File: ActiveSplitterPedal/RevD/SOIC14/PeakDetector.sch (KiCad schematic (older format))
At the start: 11 parts, among them U3 TL074

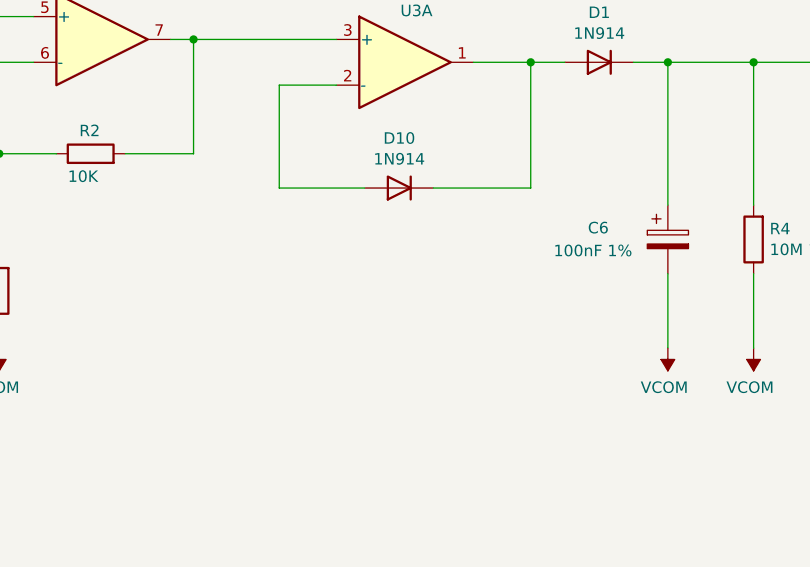
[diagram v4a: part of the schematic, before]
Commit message: updated hw
added feedback cap to peak detector (help prevent oscillation)
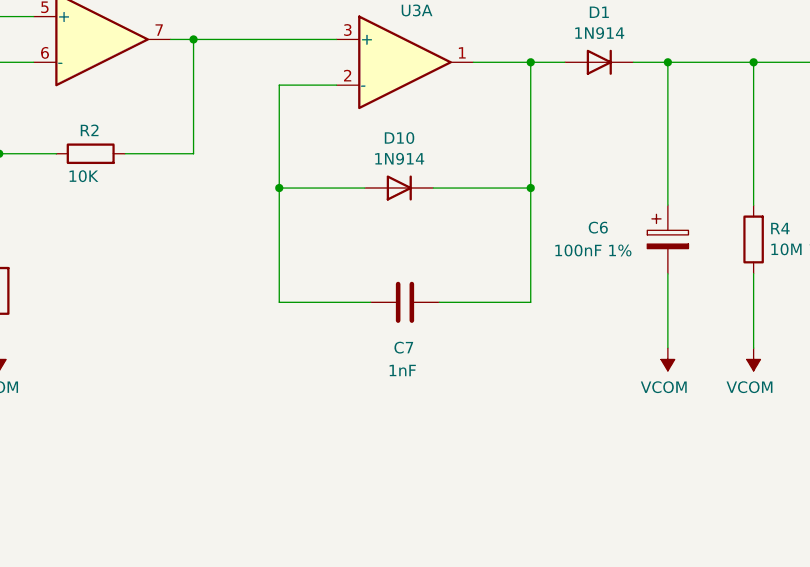
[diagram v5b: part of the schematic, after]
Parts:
- added C7: 1nF, Capacitor_SMD:C_0805_2012Metric_Pad1.15x1.40mm_HandSolder, symbol Device:C
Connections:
- net at D1.2 (A), D10.1 (K), U3.1: now also C7.1
- net at D10.2 (A), U3.2 (-): now also C7.2
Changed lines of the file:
@@
 AR Path="/5F6A4453/5F59995E" Ref="#PWR0128"  Part="1"
 AR Path="/5F6AEF1B/5F59995E" Ref="#PWR0140"  Part="1"
-F 0 "#PWR0104" H 3100 6675 50  0001 C CNN
+F 0 "#PWR0140" H 3100 6675 50  0001 C CNN
 F 1 "VCOM" H 3115 6998 50  0000 C CNN
 F 2 "" H 3100 6825 50  0001 C CNN
@@
 AR Path="/5F6A4453/5F599E65" Ref="#PWR0129"  Part="1"
 AR Path="/5F6AEF1B/5F599E65" Ref="#PWR0141"  Part="1"
-F 0 "#PWR0105" H 3600 3725 50  0001 C CNN
+F 0 "#PWR0141" H 3600 3725 50  0001 C CNN
 F 1 "VCOM" H 3615 4048 50  0000 C CNN
 F 2 "" H 3600 3875 50  0001 C CNN
@@
 AR Path="/5F6A4453/5F59A32D" Ref="#PWR0130"  Part="1"
 AR Path="/5F6AEF1B/5F59A32D" Ref="#PWR0142"  Part="1"
-F 0 "#PWR0106" H 6525 3725 50  0001 C CNN
+F 0 "#PWR0142" H 6525 3725 50  0001 C CNN
 F 1 "VCOM" H 6540 4048 50  0000 C CNN
 F 2 "" H 6525 3875 50  0001 C CNN
@@
 AR Path="/5F6A4453/5F59A89E" Ref="#PWR0131"  Part="1"
 AR Path="/5F6AEF1B/5F59A89E" Ref="#PWR0143"  Part="1"
-F 0 "#PWR0107" H 8500 3725 50  0001 C CNN
+F 0 "#PWR0143" H 8500 3725 50  0001 C CNN
 F 1 "VCOM" H 8515 4048 50  0000 C CNN
 F 2 "" H 8500 3875 50  0001 C CNN
@@
 AR Path="/5F6A4453/5F59CCEA" Ref="#PWR0132"  Part="1"
 AR Path="/5F6AEF1B/5F59CCEA" Ref="#PWR0144"  Part="1"
-F 0 "#PWR0108" H 2600 5100 50  0001 C CNN
+F 0 "#PWR0144" H 2600 5100 50  0001 C CNN
 F 1 "+3.3V" H 2615 5423 50  0000 C CNN
 F 2 "" H 2600 5250 50  0001 C CNN
@@
 AR Path="/5F6A4453/5F59E040" Ref="#PWR0133"  Part="1"
 AR Path="/5F6AEF1B/5F59E040" Ref="#PWR0145"  Part="1"
-F 0 "#PWR0109" H 2600 7000 50  0001 C CNN
+F 0 "#PWR0145" H 2600 7000 50  0001 C CNN
 F 1 "-3V3" H 2615 7073 50  0000 C CNN
 F 2 "" H 2600 6900 50  0001 C CNN
@@
 AR Path="/5F6A4453/5F59EC91" Ref="#PWR0134"  Part="1"
 AR Path="/5F6AEF1B/5F59EC91" Ref="#PWR0146"  Part="1"
-F 0 "#PWR0110" H 3100 5900 50  0001 C CNN
+F 0 "#PWR0146" H 3100 5900 50  0001 C CNN
 F 1 "VCOM" H 3115 6223 50  0000 C CNN
 F 2 "" H 3100 6050 50  0001 C CNN
@@
 AR Path="/5F6A4453/5F5FC0EE" Ref="#PWR04"  Part="1"
 AR Path="/5F6AEF1B/5F5FC0EE" Ref="#PWR05"  Part="1"
-F 0 "#PWR01" H 6900 3725 50  0001 C CNN
+F 0 "#PWR05" H 6900 3725 50  0001 C CNN
 F 1 "VCOM" H 6915 4048 50  0000 C CNN
 F 2 "" H 6900 3875 50  0001 C CNN
@@
 Wire Wire Line
 	6900 2625 7400 2625
+$Comp
+L Device:C C7
+U 1 1 5F6A8B38
+P 5375 3675
+AR Path="/5F3F1F31/5F6A8B38" Ref="C7"  Part="1"
+AR Path="/5F512144/5F6A8B38" Ref="C?"  Part="1"
+AR Path="/5F515E89/5F6A8B38" Ref="C?"  Part="1"
+AR Path="/5F519B24/5F6A8B38" Ref="C?"  Part="1"
+AR Path="/5F6A30A9/5F6A8B38" Ref="C8"  Part="1"
+AR Path="/5F6A4453/5F6A8B38" Ref="C9"  Part="1"
+AR Path="/5F6AEF1B/5F6A8B38" Ref="C10"  Part="1"
+F 0 "C7" V 5575 3625 50  0000 L CNN
+F 1 "1nF" V 5675 3600 50  0000 L CNN
+F 2 "Capacitor_SMD:C_0805_2012Metric_Pad1.15x1.40mm_HandSolder" H 5413 3525 50  0001 C CNN
+F 3 "~" H 5375 3675 50  0001 C CNN
+	1    5375 3675
+	0    1    1    0
+$EndComp
+Wire Wire Line
+	5225 3675 4825 3675
+Wire Wire Line
+	4825 3675 4825 3175
+Connection ~ 4825 3175
+Wire Wire Line
+	5525 3675 5925 3675
+Wire Wire Line
+	5925 3675 5925 3175
+Connection ~ 5925 3175
 $EndSCHEMATC
